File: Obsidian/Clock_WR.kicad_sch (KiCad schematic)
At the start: 72 parts, among them U12 LP5951MF-3.0/NOPB, U13 LM336M-2.5, U14 DAC8550IDGK, U15 DAC8550IDGK, U16 CDCM61004RHB, U3 Si5351A-B-GT, Y1 9132S-Y25.000N33DT1J, Y2 VM53S3-25.000-2.5/-30+75, Y3 OSC_20MHZ_IQD_LFVCXO026156, Y6 ABM8W-25.0000MHZ-8-D1X-T3

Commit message: removing reset global label
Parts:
- Y6: LCSC C648942 -> C6854298
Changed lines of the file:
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@@
 			)
 		)
-		(property "LCSC" "C648942"
+		(property "LCSC" "C6854298"
 			(at 177.8 133.35 0)
 			(effects

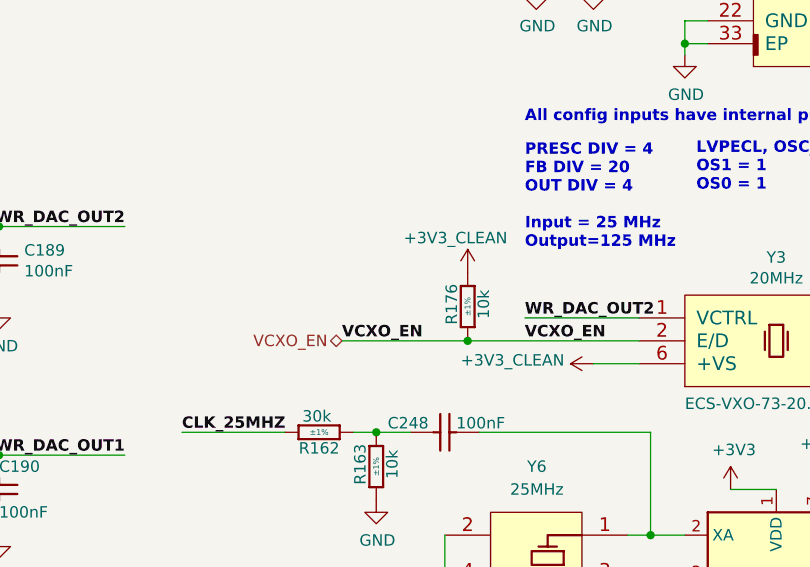
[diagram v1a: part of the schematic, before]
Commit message: adding lcsc reference for PMOD
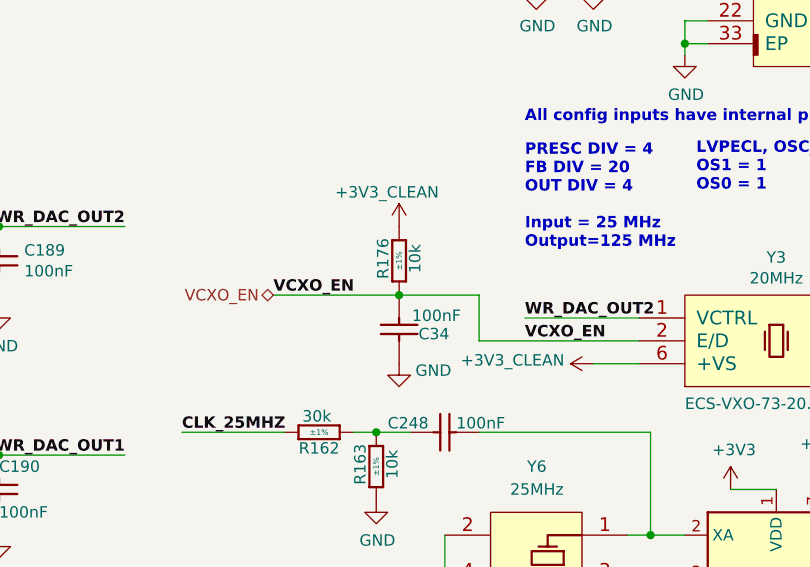
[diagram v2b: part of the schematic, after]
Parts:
- added C34: CC0402_100NF_50V_10%_X7R, Capacitor_SMD:C_0402_1005Metric, symbol Library_Symbol:CC0402_100NF_50V_10%_X7R
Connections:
- net GND: now also C34.2
- net VCXO_EN: now also C34.1
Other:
- moved on the sheet: R176

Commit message: update LCSC reference, and OFFSET rotation for JLCPCB
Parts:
- C188: footprint Capacitor_SMD:C_0402_1005Metric -> Footprint:CAPC0603X33N
- C202, C204, C205, C213, C214, C248, C34: footprint Capacitor_SMD:C_0402_1005Metric -> Footprint:CAPC1005X55N
- R102, R103, R120, R121, R99: LCSC C25094 -> C114755
- Y1: FT Rotation Offset (none) -> 270
- Y3: FT Rotation Offset 190 -> 270
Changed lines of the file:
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@@
 			)
 		)
-		(property "Footprint" "Capacitor_SMD:C_0402_1005Metric"
+		(property "Footprint" "Footprint:CAPC1005X55N"
 			(at 260.35 33.528 0)
 			(effects
@@
 			)
 		)
-		(property "Footprint" "Capacitor_SMD:C_0402_1005Metric"
+		(property "Footprint" "Footprint:CAPC1005X55N"
 			(at 251.46 151.638 0)
 			(effects
@@
 			)
 		)
-		(property "Footprint" "Capacitor_SMD:C_0402_1005Metric"
+		(property "Footprint" "Footprint:CAPC1005X55N"
 			(at 251.46 146.558 0)
 			(effects
@@
 			)
 		)
-		(property "LCSC" "C25094"
+		(property "LCSC" "C114755"
 			(at 110.49 101.6 0)
 			(effects
@@
 			)
 		)
-		(property "FT Rotation Offset" ""
+		(property "FT Rotation Offset" "270"
 			(at 105.41 22.86 0)
 			(effects
@@
 			)
 		)
-		(property "LCSC" "C25094"
+		(property "LCSC" "C114755"
 			(at 241.3 153.67 90)
 			(effects
@@
 			)
 		)
-		(property "Footprint" "Capacitor_SMD:C_0402_1005Metric"
+		(property "Footprint" "Footprint:CAPC0603X33N"
 			(at 66.802 60.96 0)
 			(effects
@@
 			)
 		)
-		(property "LCSC" "C25094"
+		(property "LCSC" "C114755"
 			(at 237.49 153.67 90)
 			(effects
@@
 			)
 		)
-		(property "Footprint" "Capacitor_SMD:C_0402_1005Metric"
+		(property "Footprint" "Footprint:CAPC1005X55N"
 			(at 149.352 109.22 0)
 			(effects
@@
 			)
 		)
-		(property "Footprint" "Capacitor_SMD:C_0402_1005Metric"
+		(property "Footprint" "Footprint:CAPC1005X55N"
 			(at 166.37 132.588 0)
 			(effects
@@
 			)
 		)
-		(property "LCSC" "C25094"
+		(property "LCSC" "C114755"
 			(at 60.96 157.48 90)
 			(effects
@@
 			)
 		)
-		(property "Footprint" "Capacitor_SMD:C_0402_1005Metric"
+		(property "Footprint" "Footprint:CAPC1005X55N"
 			(at 260.35 36.068 0)
 			(effects
@@
 			)
 		)
-		(property "LCSC" "C25094"
+		(property "LCSC" "C114755"
 			(at 110.49 127 0)
 			(effects
@@
 			)
 		)
-		(property "FT Rotation Offset" "190"
+		(property "FT Rotation Offset" "270"
 			(at 189.23 109.22 0)
 			(effects
@@
 			)
 		)
-		(property "Footprint" "Capacitor_SMD:C_0402_1005Metric"
+		(property "Footprint" "Footprint:CAPC1005X55N"
 			(at 184.15 26.162 0)
 			(effects

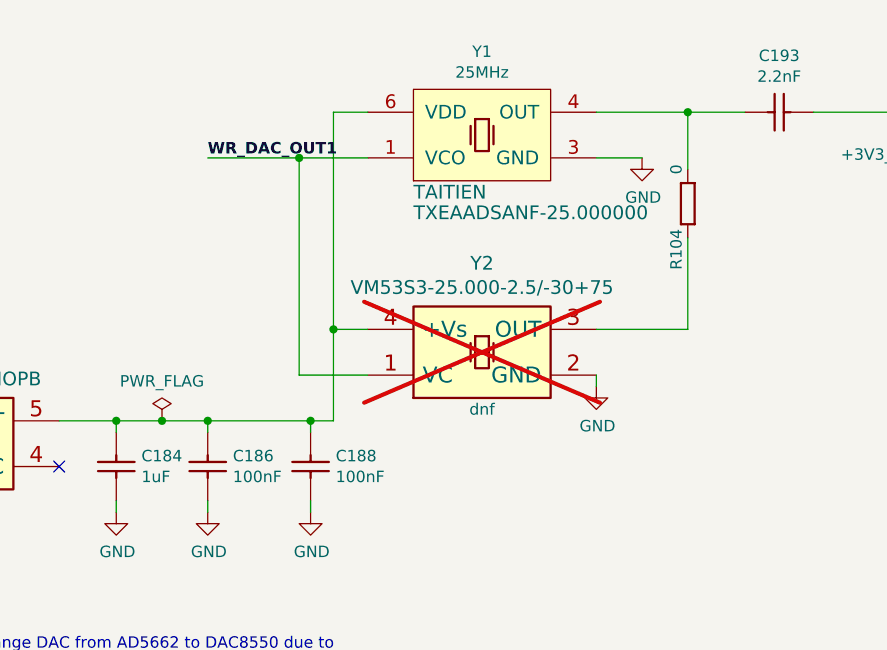
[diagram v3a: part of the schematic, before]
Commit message: Replacing oscillators with CMOS output oscillator
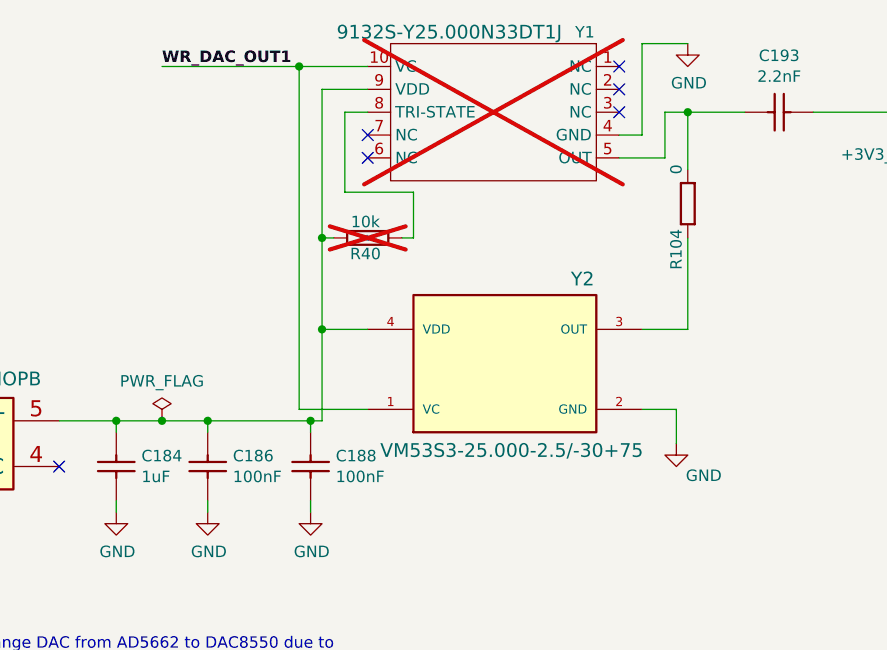
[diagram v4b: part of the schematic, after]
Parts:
- added R40: R0402_10K_1%_0.0625W_100PPM, Footprint:RESC1005X40N, symbol Library_Symbol:R0402_10K_1%_0.0625W_100PPM
- Y1: footprint Footprint:OSC_ABRACON_ASEMPC -> Footprint:OSC-SMD_10P-L7.0-W5.0-BL_OHXXXXXXX; symbol Library_Symbol:OSC_25MHZ_RAKON_IVT3205CR -> Library_Symbol:9875HA-25.000N33FT1JL; LCSC C52954962 -> C20754707; LCSC Part Name (none) -> 25MHz ±1ppm 3.3V; Manufacturer TAITIEN -> HCI(杭晶); Manufacturer Part (none) -> 9875HA-25.000N33FT1JL; Supplier (none) -> LCSC; now not fitted; now left out of the parts list
- Y2: footprint Footprint:OSCCC320X500X160-4N -> Footprint:OSC_SIT5001AC-GE-33VQ-25.000000X; symbol Library_Symbol:Oscillator_1VC_2GND_3OUT_4+Vs-clocks-SchDoc-cache -> Library_Symbol:SIT5001AC-GE-33VQ-25.000000X; Availability (none) -> In Stock; Check_prices (none) -> https://www.snapeda.com/parts/SIT5001AC-GE-33VQ-25.000000X/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; Description_1 (none) -> 25 MHz VCTCXO LVCMOS Oscillator 3.3V 4-SMD, No Lead; MANUFACTURER (none) -> SITIME; MAXIMUM_PACKAGE_HEIGHT (none) -> 0.8 mm; MF (none) -> SiTime; MP (none) -> SIT5001AC-GE-33VQ-25.000000X; PARTREV (none) -> NA; Package (none) -> NON STANDARD-4 Rochester Electronics; Price (none) -> None; STANDARD (none) -> Manufacturer Recommendations; SnapEDA_Link (none) -> https://www.snapeda.com/parts/SIT5001AC-GE-33VQ-25.000000X/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; now fitted
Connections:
- net GND: now also Y1.4 (GND); no longer Y1.3 (GND)
- net WR_DAC_OUT1: now also Y1.10 (VC); no longer Y1.1 (VCO)
- net at C184.1, C186.1, C188.1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: now also Y1.9 (VDD), R40.2; no longer Y1.6 (VDD)
- net at C193.1, R104.2: now also Y1.5 (OUT); no longer Y1.4 (OUT)
- new net: R40.1, Y1.8 (TRI-STATE)
- no-connect marks 10 -> 15

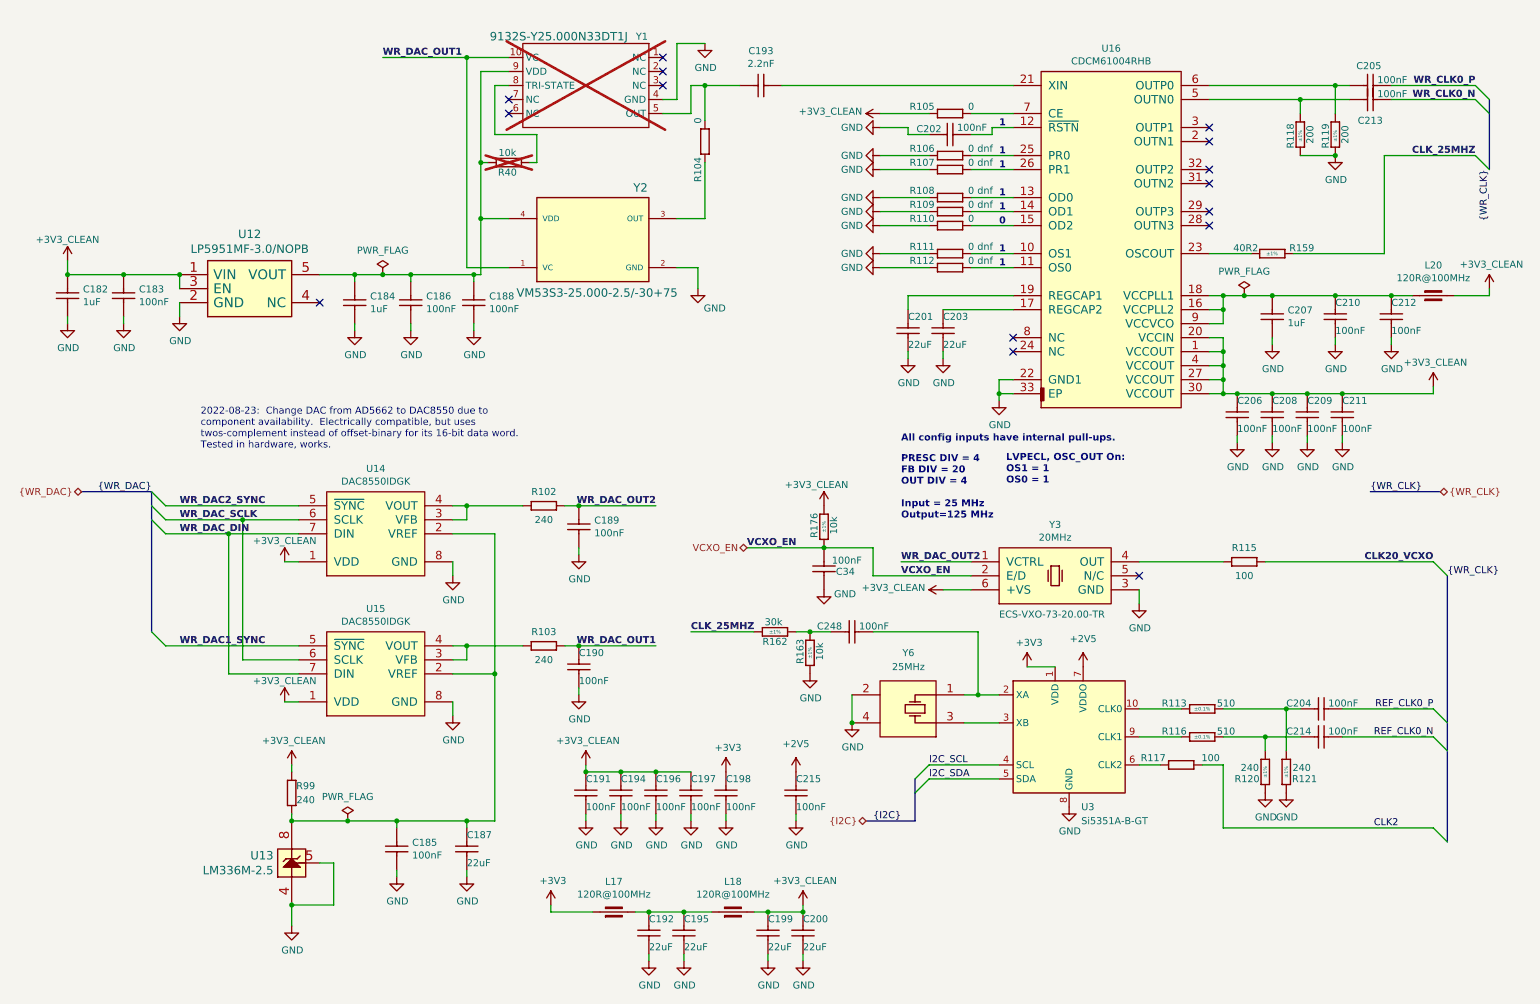
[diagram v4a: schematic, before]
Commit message: Update the components around U16, see #9
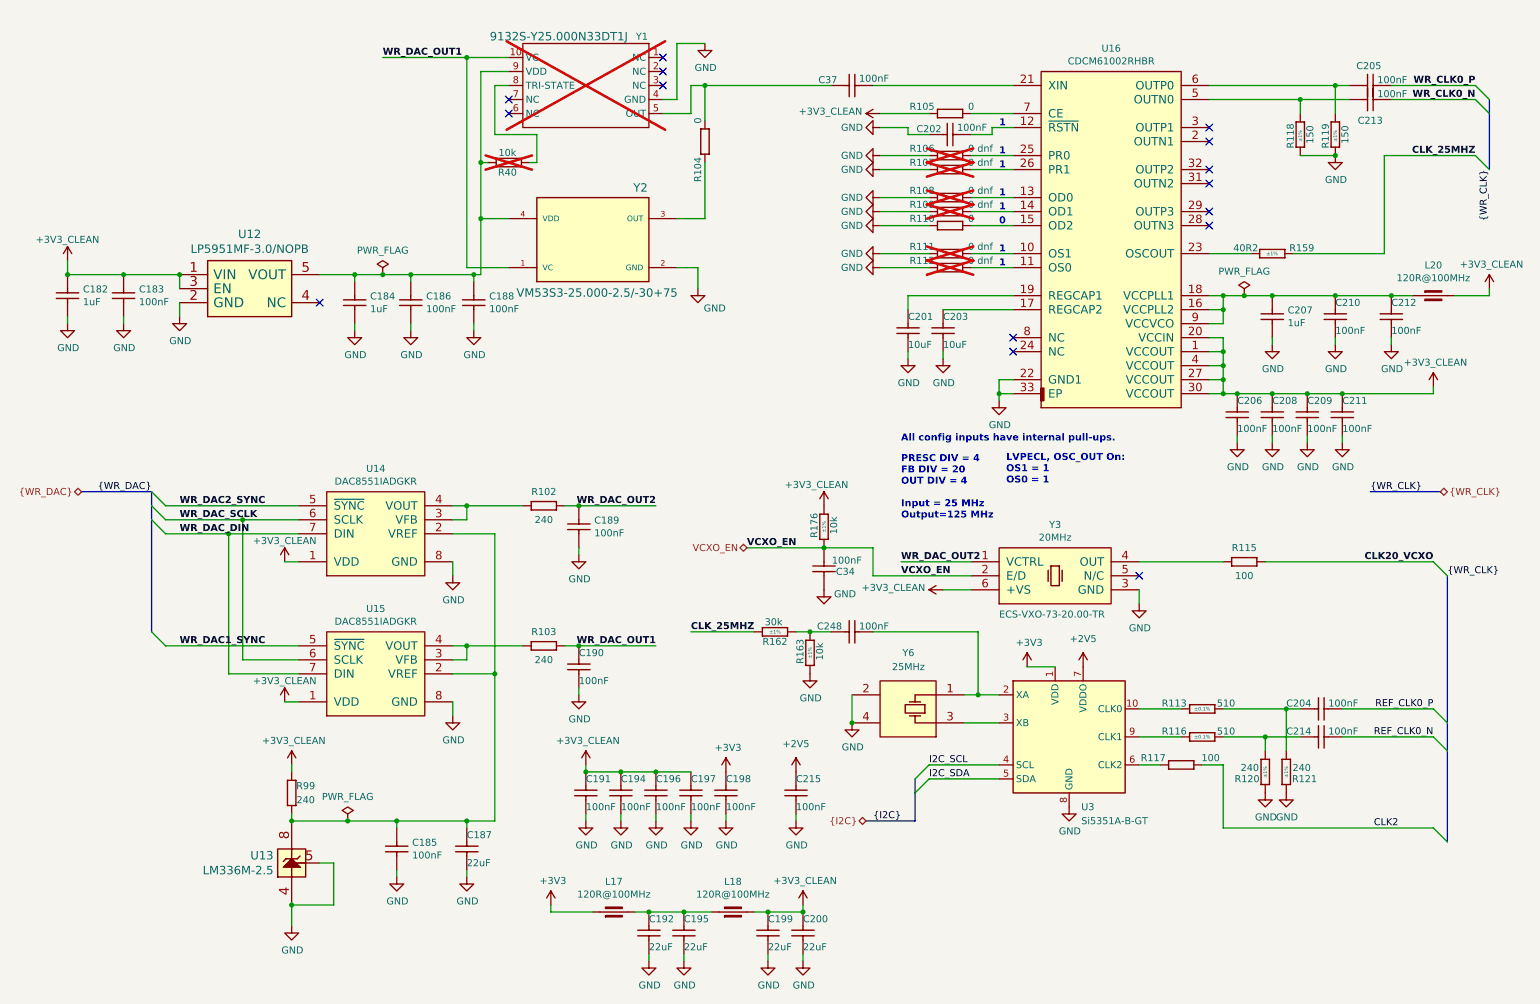
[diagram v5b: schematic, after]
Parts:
- removed C193: CC0402_2.2NF_50V_10%_X7R, Capacitor_SMD:C_0402_1005Metric, symbol Library_Symbol:CC0402_2.2NF_50V_10%_X7R
- added C37: CC0402_100NF_50V_10%_X7R, Footprint:CAPC1005X55N, symbol Library_Symbol:CC0402_100NF_50V_10%_X7R
- C201, C203: value CC0603_22UF_6.3V_20%_X5R -> CC0603_10UF_6.3V_20%_Y5V; LCSC C59461 -> C138601; Val 22uF -> 10uF; ~ 22uF -> 10uF
- R106, R107, R108, R109, R111, R112: now not fitted; now left out of the parts list
- R118, R119: value R0402_200R_1%_0.0625W_100PPM -> R0402_150R_1%_0.0625W_100PPM; Comment 200 -> 150; LCSC C114764 -> C138054; Manufacturer Part Number R0402_200R_1%_0.0625W_100PPM -> R0402_150R_1%_0.0625W_100PPM; Val 200 -> 150
- U14, U15: value DAC8550IDGK -> DAC8551IADGKR
- U16: value CDCM61004RHB -> CDCM61002RHBR
- Y1: footprint Footprint:OSC-SMD_10P-L7.0-W5.0-BL_OHXXXXXXX -> ProLib_pcs_2026-03-30:OSC-SMD_10P-L7.0-W5.0-BL_OHXXXXXXX
- Y2: LCSC (none) -> C1988162; config dnf -> (none)
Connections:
- net at R104.2, Y1.5 (OUT): now also C37.2
- net at U16.21 (XIN): now also C37.1
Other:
- note removed: "2022-08-23: Change DAC from AD5662 to DAC8550 due to component availability. Electrically compatible, but uses twos-complement instead of offset-binary for its 16-bit data word. Tested in hardware, works."
